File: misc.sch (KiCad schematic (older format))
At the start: 5 parts, among them J13 MICROSD_SLOT_TFP09-2-12B

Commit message: more schematics
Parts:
- added C? (x5): 10uF, symbol C_Small
- added P?: CONN_02X05, symbol CONN_02X05
- added P?: CONN_01X05, symbol CONN_01X05
- added R? (x5): 4K7, symbol RESISTOR
- added U?: 24LC256, symbol 24C16
- J13: footprint (none) -> geda-footprints:MICROSD_SLOT_TFP09-2-12B
- R32, R33, R34: footprint (none) -> Resistors_SMD:R_0603
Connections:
- net +3V3: now also P?.1 (P1), P?.2 (P2), P?.3 (P3), P?.4 (P4), P?.5 (P5), R?.1, R?.1, R?.1, R?.1, R?.1, U?.8 (VCC)
- net GND: now also C?.2, C?.2, C?.2, C?.2, C?.2, P?.10 (P10), P?.2 (P2), P?.4 (P4), P?.6 (P6), P?.8 (P8), U?.1 (A0), U?.2 (A1), U?.3 (A2), U?.4 (GND), U?.7 (WP)
- new net: C?.1, P?.1 (P1), R?.2
- new net: C?.1, P?.3 (P3), R?.2
- new net: C?.1, P?.5 (P5), R?.2
- new net: C?.1, P?.7 (P7), R?.2
- new net: C?.1, P?.9 (P9), R?.2

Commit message: More schematics, some layout
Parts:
- added C19, C20, C21, C22, C23, C24, C25: 100nF, Capacitors_SMD:C_0603, symbol C_Small
- added P13: EXT_SD, geda-footprints:CON_HDR_2x5, symbol CONN_02X05
- added P14: LCD, geda-footprints:CON_HDR_2x5, symbol CONN_02X05
- added P15: LIMIT_SWITCHES, geda-footprints:CON_HDR_2x7, symbol CONN_02X07
- added P16: LIMIT_SWITCHES_V, geda-footprints:CON_HDR_1x7, symbol CONN_01X07
- added P17, P18, P19, P20: CONN_01X03, geda-footprints:CON_HDR_1x3, symbol CONN_01X03
- added R35, R36: 4K7, Resistors_SMD:R_0603, symbol RESISTOR
- C26, C27, C28, C29, C30: renamed from C?; footprint (none) -> Capacitors_SMD:C_0805
- P21: renamed from P?; value CONN_02X05 -> THERMISTORS; footprint (none) -> geda-footprints:CON_HDR_2x5
- P22: renamed from P?; footprint (none) -> geda-footprints:CON_HDR_1x5
- R37, R38, R39, R40, R41: renamed from R?; footprint (none) -> Resistors_SMD:R_0603
- U2: renamed from U?; footprint (none) -> geda-footprints:SOIC8
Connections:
- net +3V3: now also P13.8 (P8), P16.1 (P1), P16.2 (P2), P16.3 (P3), P16.4 (P4), P16.5 (P5), P16.6 (P6), P16.7 (P7), P17.2 (P2), P18.2 (P2), P19.2 (P2), P20.2 (P2)
- net GND: now also C19.2, C20.2, C21.2, C22.2, C23.2, C24.2, C25.2, P13.2 (P2), P14.2 (P2), P15.10 (P10), P15.12 (P12), P15.14 (P14), P15.2 (P2), P15.4 (P4), P15.6 (P6), P15.8 (P8), P17.1 (P1), P18.1 (P1), P19.1 (P1), P20.1 (P1)
- net SD_CS: no longer J13.9 (CD0)
- net SD_MISO: now also P13.5 (P5)
- net SD_MOSI: now also P13.6 (P6)
- net SD_SCK: now also P13.4 (P4)
- net T0: now reaches C26.1, P21.1 (P1), R37.2
- net T1: now reaches C27.1, P21.3 (P3), R38.2
- net T2: now reaches C28.1, P21.5 (P5), R39.2
- net T3: now reaches C29.1, P21.7 (P7), R40.2
- net T4: now reaches C30.1, P21.9 (P9), R41.2
- net SDA1: now reaches U2.5 (SDA)
- net SDA1: now also R36.2
- net SCL1: now reaches U2.6 (SCL)
- net SCL1: now also R35.2
- new net: R35.1, R36.1
- new net +5V: P14.1 (P1)
- new net AUX-1: P17.3 (P3)
- new net AUX-2: P18.3 (P3)
- new net AUX-3: P19.3 (P3)
- new net AUX-4: P20.3 (P3)
- new net ENC-A: P14.3 (P3)
- new net ENC-B: P14.4 (P4)
- new net ENC-SW: P13.7 (P7)
- new net LCD_D4: P14.10 (P10)
- new net LCD_D5: P14.5 (P5)
- new net LCD_D6: P14.7 (P7)
- new net LCD_D7: P14.9 (P9)
- new net LCD_E: P14.8 (P8)
- new net LCD_RS: P14.6 (P6)
- new net PROBE: C19.1, P15.13 (P13)
- new net SD2_CS: P13.3 (P3)
- new net SD_CD: J13.9 (CD0)
- new net X+: C24.1, P15.3 (P3)
- new net X-: C25.1, P15.1 (P1)
- new net Y+: C22.1, P15.7 (P7)
- new net Y-: C23.1, P15.5 (P5)
- new net Z+: C20.1, P15.11 (P11)
- new net Z-: C21.1, P15.9 (P9)
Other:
- moved on the sheet: C26, C27, C28, C29, C30, P21, P22, R37, R38, R39, R40, R41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

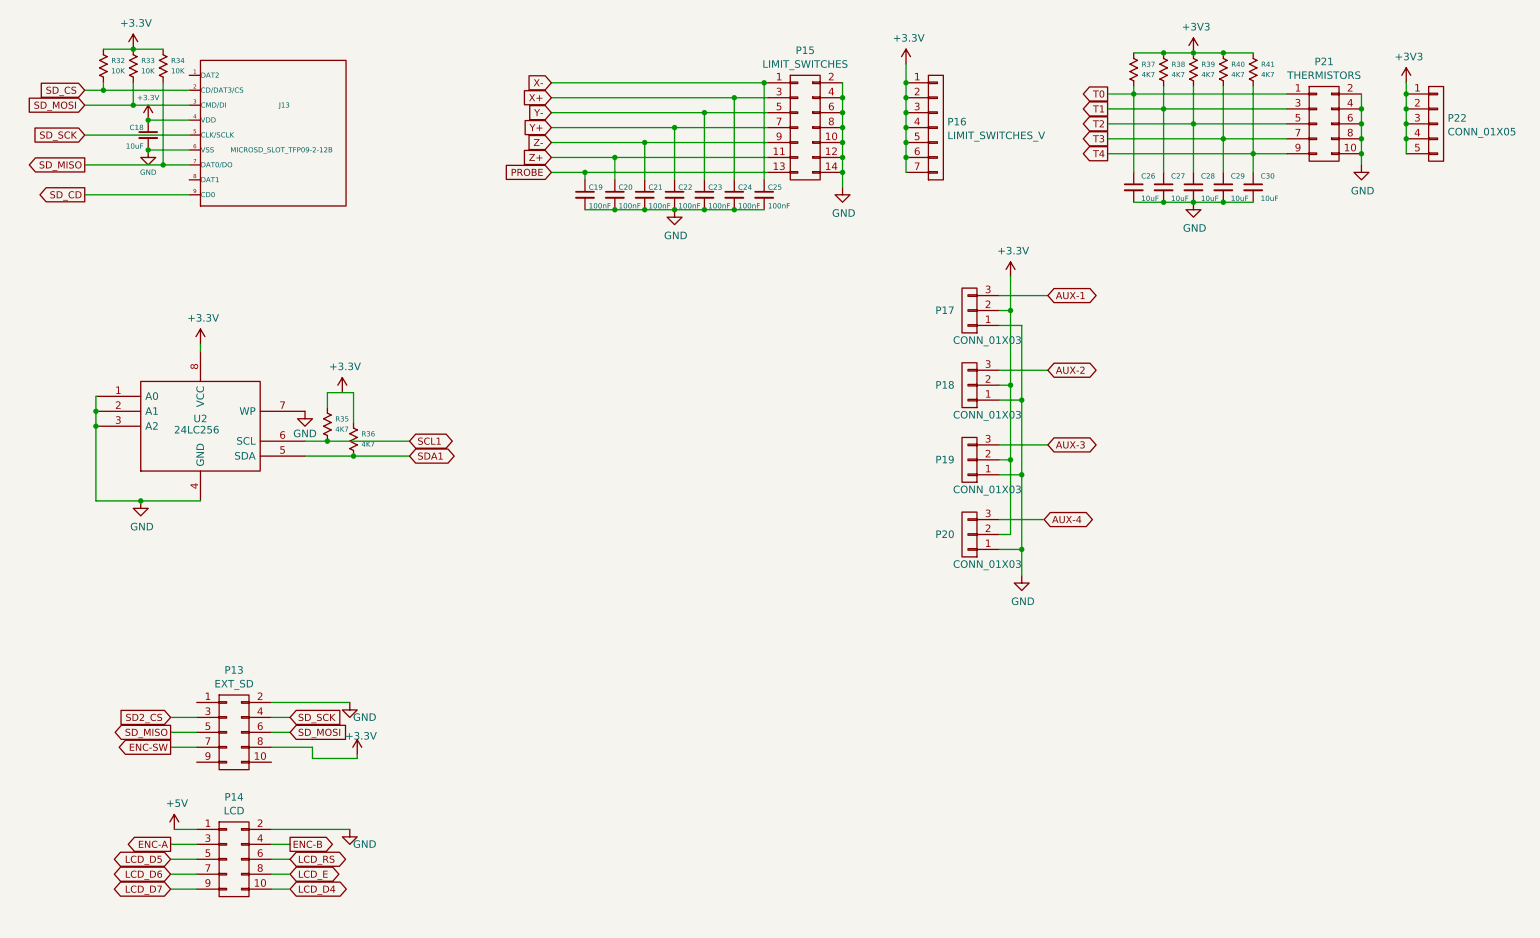
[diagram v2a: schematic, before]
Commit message: more placement and routing
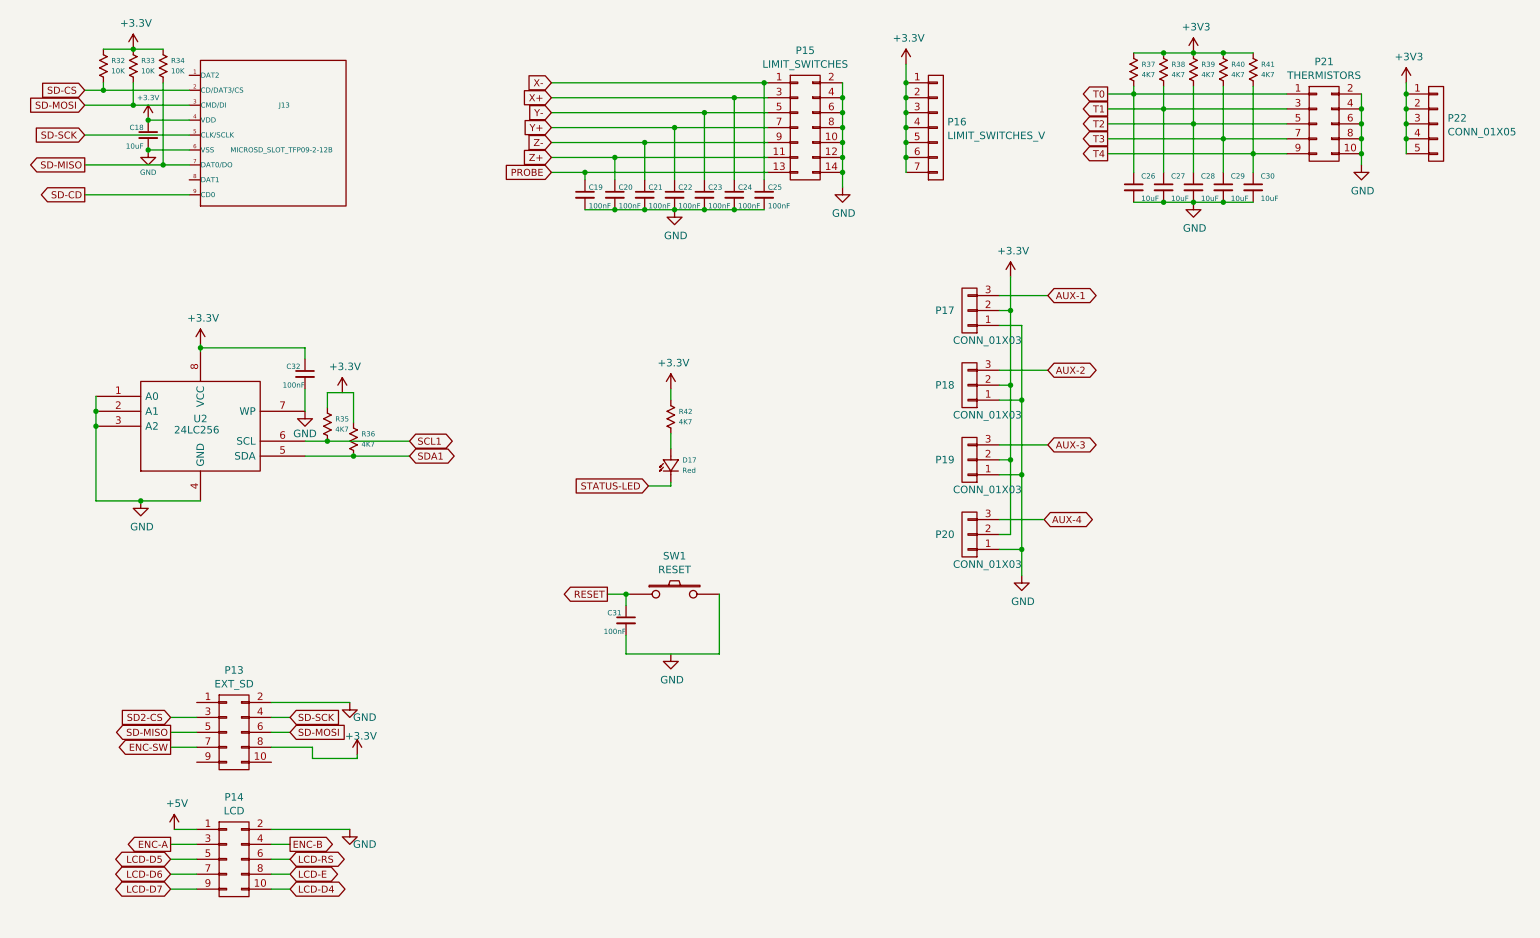
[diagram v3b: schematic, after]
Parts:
- added C31, C32: 100nF, Capacitors_SMD:C_0603, symbol C_Small
- added D17: Red, geda-footprints:0603diode, symbol Red
- added R42: 4K7, Resistors_SMD:R_0603, symbol RESISTOR
- added SW1: RESET, geda-footprints:BUTTON_PUSH_SMD_6x6mm, symbol SW_PUSH
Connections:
- net +3V3: now also C32.1, R42.1
- net GND: now also C32.2
- net LCD_D4 renamed LCD-D4
- net LCD_D5 renamed LCD-D5
- net LCD_D6 renamed LCD-D6
- net LCD_D7 renamed LCD-D7
- net LCD_E renamed LCD-E
- net LCD_RS renamed LCD-RS
- net SD2_CS renamed SD2-CS
- net SD_CD renamed SD-CD
- net SD_CS renamed SD-CS
- net SD_MISO renamed SD-MISO
- net SD_MOSI renamed SD-MOSI
- net SD_SCK renamed SD-SCK
- new net: D17.1 (null), R42.2
- new net: C31.2, SW1.2
- new net RESET: C31.1, SW1.1
- new net STATUS-LED: D17.2 (null)
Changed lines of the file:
@@
 EESchema Schematic File Version 2
+LIBS:led_reverse
 LIBS:arduino_shieldsNCL
 LIBS:otheruse_transistors
@@
 $EndDescr
 Text GLabel 1400 1575 0    47   Input ~ 0
-SD_CS
+SD-CS
 Text GLabel 1400 1675 0    47   Input ~ 0
-SD_MOSI
+SD-MOSI
 Text GLabel 1400 2075 0    47   Output ~ 0
-SD_MISO
+SD-MISO
 Text GLabel 1400 1875 0    47   Input ~ 0
-SD_SCK
+SD-SCK
 $Comp
 L RESISTOR R32
@@
 $EndComp
 $Comp
-L +3.3V #PWR074
+L +3.3V #PWR083
 U 1 1 568CFCD8
 P 1725 1300
-F 0 "#PWR074" H 1725 1150 50  0001 C CNN
+F 0 "#PWR083" H 1725 1150 50  0001 C CNN
 F 1 "+3.3V" H 1743 1474 50  0000 C CNN
 F 2 "" H 1725 1300 50  0000 C CNN
@@
 $EndComp
 $Comp
-L +3.3V #PWR075
+L +3.3V #PWR084
 U 1 1 568CFFAF
 P 1825 1775
-F 0 "#PWR075" H 1825 1625 50  0001 C CNN
+F 0 "#PWR084" H 1825 1625 50  0001 C CNN
 F 1 "+3.3V" H 1825 1925 35  0000 C CNN
 F 2 "" H 1825 1775 50  0000 C CNN
@@
 $EndComp
 Text GLabel 1400 2275 0    47   Output ~ 0
-SD_CD
+SD-CD
 $Comp
 L MICROSD_SLOT_TFP09-2-12B J13
@@
 $EndComp
 $Comp
-L GND #PWR076
+L GND #PWR085
 U 1 1 568C59D5
 P 1825 1975
-F 0 "#PWR076" H 1825 1725 50  0001 C CNN
+F 0 "#PWR085" H 1825 1725 50  0001 C CNN
 F 1 "GND" H 1825 1825 35  0000 C CNN
 F 2 "" H 1825 1975 50  0000 C CNN
@@
 $EndComp
 $Comp
-L GND #PWR077
+L GND #PWR086
 U 1 1 568D834C
 P 9950 2075
-F 0 "#PWR077" H 9950 1825 50  0001 C CNN
+F 0 "#PWR086" H 9950 1825 50  0001 C CNN
 F 1 "GND" H 9958 1901 50  0000 C CNN
 F 2 "" H 9950 2075 50  0000 C CNN
@@
 $EndComp
 $Comp
-L GND #PWR078
+L GND #PWR087
 U 1 1 568D94E5
 P 8825 2325
-F 0 "#PWR078" H 8825 2075 50  0001 C CNN
+F 0 "#PWR087" H 8825 2075 50  0001 C CNN
 F 1 "GND" H 8833 2151 50  0000 C CNN
 F 2 "" H 8825 2325 50  0000 C CNN
@@
 $EndComp
 $Comp
-L +3V3 #PWR079
+L +3V3 #PWR088
 U 1 1 568D9512
 P 8825 1325
-F 0 "#PWR079" H 8825 1175 50  0001 C CNN
+F 0 "#PWR088" H 8825 1175 50  0001 C CNN
 F 1 "+3V3" H 8843 1499 50  0000 C CNN
 F 2 "" H 8825 1325 50  0000 C CNN
@@
 $EndComp
 $Comp
-L +3V3 #PWR080
+L +3V3 #PWR089
 U 1 1 568D9A56
 P 10250 1525
-F 0 "#PWR080" H 10250 1375 50  0001 C CNN
+F 0 "#PWR089" H 10250 1375 50  0001 C CNN
 F 1 "+3V3" H 10268 1699 50  0000 C CNN
 F 2 "" H 10250 1525 50  0000 C CNN
@@
 $EndComp
 $Comp
-L GND #PWR081
+L GND #PWR090
 U 1 1 568DA443
 P 2875 3725
-F 0 "#PWR081" H 2875 3475 50  0001 C CNN
+F 0 "#PWR090" H 2875 3475 50  0001 C CNN
 F 1 "GND" H 2875 3575 50  0000 C CNN
 F 2 "" H 2875 3725 50  0000 C CNN
@@
 $EndComp
 $Comp
-L GND #PWR082
+L GND #PWR091
 U 1 1 568DA52A
 P 1775 4325
-F 0 "#PWR082" H 1775 4075 50  0001 C CNN
+F 0 "#PWR091" H 1775 4075 50  0001 C CNN
 F 1 "GND" H 1783 4151 50  0000 C CNN
 F 2 "" H 1775 4325 50  0000 C CNN
@@
 $EndComp
 $Comp
-L +3.3V #PWR083
+L +3.3V #PWR092
 U 1 1 568DA65A
 P 2175 3275
-F 0 "#PWR083" H 2175 3125 50  0001 C CNN
+F 0 "#PWR092" H 2175 3125 50  0001 C CNN
 F 1 "+3.3V" H 2193 3449 50  0000 C CNN
 F 2 "" H 2175 3275 50  0000 C CNN
@@
 $EndComp
 $Comp
-L GND #PWR084
+L GND #PWR093
 U 1 1 568D90A7
 P 6475 2225
-F 0 "#PWR084" H 6475 1975 50  0001 C CNN
+F 0 "#PWR093" H 6475 1975 50  0001 C CNN
 F 1 "GND" H 6483 2051 50  0000 C CNN
 F 2 "" H 6475 2225 50  0000 C CNN
@@
 $EndComp
 $Comp
-L +3.3V #PWR085
+L +3.3V #PWR094
 U 1 1 568D9133
 P 6900 1400
-F 0 "#PWR085" H 6900 1250 50  0001 C CNN
+F 0 "#PWR094" H 6900 1250 50  0001 C CNN
 F 1 "+3.3V" H 6918 1574 50  0000 C CNN
 F 2 "" H 6900 1400 50  0000 C CNN
@@
 $EndComp
 $Comp
-L GND #PWR086
+L GND #PWR095
 U 1 1 568DAACD
 P 5350 2375
-F 0 "#PWR086" H 5350 2125 50  0001 C CNN
+F 0 "#PWR095" H 5350 2125 50  0001 C CNN
 F 1 "GND" H 5358 2201 50  0000 C CNN
 F 2 "" H 5350 2375 50  0000 C CNN
@@
 $EndComp
 $Comp
-L +3.3V #PWR087
+L +3.3V #PWR096
 U 1 1 568E82EF
 P 3125 3600
-F 0 "#PWR087" H 3125 3450 50  0001 C CNN
+F 0 "#PWR096" H 3125 3450 50  0001 C CNN
 F 1 "+3.3V" H 3143 3774 50  0000 C CNN
 F 2 "" H 3125 3600 50  0000 C CNN
@@
 	7600 4550 7525 4550
 $Comp
-L GND #PWR088
+L GND #PWR097
 U 1 1 568EABC9
 P 7675 4825
-F 0 "#PWR088" H 7675 4575 50  0001 C CNN
+F 0 "#PWR097" H 7675 4575 50  0001 C CNN
 F 1 "GND" H 7683 4651 50  0000 C CNN
 F 2 "" H 7675 4825 50  0000 C CNN
@@
 $EndComp
 $Comp
-L +3.3V #PWR089
+L +3.3V #PWR098
 U 1 1 568EAEBC
 P 7600 2825
-F 0 "#PWR089" H 7600 2675 50  0001 C CNN
+F 0 "#PWR098" H 7600 2675 50  0001 C CNN
 F 1 "+3.3V" H 7618 2999 50  0000 C CNN
 F 2 "" H 7600 2825 50  0000 C CNN
@@
 $EndComp
 Text GLabel 1975 5775 0    47   Input ~ 0
-SD2_CS
+SD2-CS
 Text GLabel 2775 5875 2    47   Input ~ 0
-SD_MOSI
+SD-MOSI
 Text GLabel 1975 5875 0    47   Output ~ 0
-SD_MISO
+SD-MISO
 Text GLabel 2775 5775 2    47   Input ~ 0
-SD_SCK
-$Comp
-L GND #PWR090
+SD-SCK
+$Comp
+L GND #PWR099
 U 1 1 568F027E
 P 3175 5675
-F 0 "#PWR090" H 3175 5425 50  0001 C CNN
+F 0 "#PWR099" H 3175 5425 50  0001 C CNN
 F 1 "GND" H 3275 5575 50  0000 C CNN
 F 2 "" H 3175 5675 50  0000 C CNN
@@
 	2650 5675 3175 5675
 $Comp
-L +3.3V #PWR091
+L +3.3V #PWR0100
 U 1 1 568F1103
 P 3225 6025
-F 0 "#PWR091" H 3225 5875 50  0001 C CNN
+F 0 "#PWR0100" H 3225 5875 50  0001 C CNN
 F 1 "+3.3V" H 3250 6150 50  0000 C CNN
 F 2 "" H 3225 6025 50  0000 C CNN
@@
 	3225 6050 3225 6025
 $Comp
-L +5V #PWR092
+L +5V #PWR0101
 U 1 1 568F17B3
 P 2000 6525
-F 0 "#PWR092" H 2000 6375 50  0001 C CNN
+F 0 "#PWR0101" H 2000 6375 50  0001 C CNN
 F 1 "+5V" H 2018 6699 50  0000 C CNN
 F 2 "" H 2000 6525 50  0000 C CNN
@@
 $EndComp
 $Comp
-L GND #PWR093
+L GND #PWR0102
 U 1 1 568F18BA
 P 3175 6525
-F 0 "#PWR093" H 3175 6275 50  0001 C CNN
+F 0 "#PWR0102" H 3175 6275 50  0001 C CNN
 F 1 "GND" H 3275 6425 50  0000 C CNN
 F 2 "" H 3175 6525 50  0000 C CNN
@@
 	2150 6625 1975 6625
 Text GLabel 1975 6725 0    47   BiDi ~ 0
-LCD_D5
+LCD-D5
 Text GLabel 1975 6825 0    47   BiDi ~ 0
-LCD_D6
+LCD-D6
 Text GLabel 1975 6925 0    47   BiDi ~ 0
-LCD_D7
+LCD-D7
 Text GLabel 2775 6925 2    47   BiDi ~ 0
-LCD_D4
+LCD-D4
 Text GLabel 2775 6825 2    47   BiDi ~ 0
-LCD_E
+LCD-E
 Text GLabel 2775 6725 2    47   BiDi ~ 0
-LCD_RS
+LCD-RS
 Wire Wire Line
 	1975 6725 2150 6725
@@
 Text GLabel 8250 2000 0    47   Output ~ 0
 T4
+$Comp
+L Red D17
+U 1 1 568F7EEA
+P 5375 4200
+F 0 "D17" V 5523 4173 34  0000 R CNN
+F 1 "Red" V 5454 4173 34  0000 R CNN
+F 2 "geda-footprints:0603diode" H 5375 4200 60  0001 C CNN
+F 3 "" H 5375 4200 60  0000 C CNN
+	1    5375 4200
+	0    -1   -1   0
+$EndComp
+$Comp
+L SW_PUSH SW1
+U 1 1 568F83A9
+P 5350 4950
+F 0 "SW1" H 5350 5206 50  0000 C CNN
+F 1 "RESET" H 5350 5114 50  0000 C CNN
+F 2 "geda-footprints:BUTTON_PUSH_SMD_6x6mm" H 5350 4950 50  0001 C CNN
+F 3 "" H 5350 4950 50  0000 C CNN
+	1    5350 4950
+	1    0    0    -1
+$EndComp
+Text GLabel 5175 4225 0    47   Input ~ 0
+STATUS-LED
+$Comp
+L RESISTOR R42
+U 1 1 568F903C
+P 5300 3650
+F 0 "R42" V 5377 3728 34  0000 L CNN
+F 1 "4K7" V 5446 3728 34  0000 L CNN
+F 2 "Resistors_SMD:R_0603" H 5300 3650 60  0001 C CNN
+F 3 "" H 5300 3650 60  0000 C CNN
+	1    5300 3650
+	0    1    1    0
+$EndComp
+Wire Wire Line
+	5325 3875 5325 3975
+Wire Wire Line
+	5175 4225 5325 4225
+Wire Wire Line
+	5325 4225 5325 4200
+$Comp
+L +3.3V #PWR0103
+U 1 1 568F9643
+P 5325 3575
+F 0 "#PWR0103" H 5325 3425 50  0001 C CNN
+F 1 "+3.3V" H 5343 3749 50  0000 C CNN
+F 2 "" H 5325 3575 50  0000 C CNN
+F 3 "" H 5325 3575 50  0000 C CNN
+	1    5325 3575
+	1    0    0    -1
+$EndComp
+Wire Wire Line
+	5325 3575 5325 3650
+Text GLabel 4900 4950 0    47   Output ~ 0
+RESET
+Wire Wire Line
+	4900 4950 5050 4950
+$Comp
+L GND #PWR0104
+U 1 1 568F9E88
+P 5325 5350
+F 0 "#PWR0104" H 5325 5100 50  0001 C CNN
+F 1 "GND" H 5333 5176 50  0000 C CNN
+F 2 "" H 5325 5350 50  0000 C CNN
+F 3 "" H 5325 5350 50  0000 C CNN
+	1    5325 5350
+	1    0    0    -1
+$EndComp
+$Comp
+L C_Small C31
+U 1 1 568FA294
+P 5025 5125
+F 0 "C31" H 4900 5175 35  0000 L CNN
+F 1 "100nF" H 4875 5050 35  0000 L CNN
+F 2 "Capacitors_SMD:C_0603" H 5025 5125 50  0001 C CNN
+F 3 "" H 5025 5125 50  0000 C CNN
+	1    5025 5125
+	1    0    0    -1
+$EndComp
+Wire Wire Line
+	5025 5025 5025 4950
+Connection ~ 5025 4950
+Wire Wire Line
+	5025 5225 5025 5350
+Wire Wire Line
+	5025 5350 5650 5350
+Wire Wire Line
+	5650 5350 5650 4950
+$Comp
+L C_Small C32
+U 1 1 568FAA2A
+P 2875 3475
+F 0 "C32" H 2750 3525 35  0000 L CNN
+F 1 "100nF" H 2725 3400 35  0000 L CNN
+F 2 "Capacitors_SMD:C_0603" H 2875 3475 50  0001 C CNN
+F 3 "" H 2875 3475 50  0000 C CNN
+	1    2875 3475
+	1    0    0    -1
+$EndComp
+Wire Wire Line
+	2875 3575 2875 3725
+Wire Wire Line
+	2875 3300 2875 3375
+Wire Wire Line
+	2875 3300 2175 3300
+Connection ~ 2175 3300
 $EndSCHEMATC

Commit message: More routing
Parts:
- added C33: 10uF, Capacitors_SMD:C_0805, symbol C_Small
- D17: footprint geda-footprints:0603diode -> armin-footprints:0603diode
- U2: footprint geda-footprints:SOIC8 -> armin-footprints:SOIC8
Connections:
- net +3V3: now also P17.1 (P1), P18.1 (P1), P19.1 (P1), P20.1 (P1), R35.1, R36.1, C33.1; no longer P17.2 (P2), P18.2 (P2), P19.2 (P2), P20.2 (P2)
- net GND: now also P17.2 (P2), P18.2 (P2), P19.2 (P2), P20.2 (P2), C33.2; no longer P17.1 (P1), P18.1 (P1), P19.1 (P1), P20.1 (P1)
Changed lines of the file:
@@
 F 0 "U2" H 2175 3875 50  0000 C CNN
 F 1 "24LC256" H 2150 3800 50  0000 C CNN
-F 2 "geda-footprints:SOIC8" H 2175 3825 50  0001 C CNN
+F 2 "armin-footprints:SOIC8" H 2175 3825 50  0001 C CNN
 F 3 "" H 2175 3825 50  0000 C CNN
 	1    2175 3825
@@
 U 1 1 568D8D39
 P 6225 1825
-F 0 "P15" H 6225 2341 50  0000 C CNN
-F 1 "LIMIT_SWITCHES" H 6225 2249 50  0000 C CNN
+F 0 "P15" H 6225 2300 50  0000 C CNN
+F 1 "LIMIT_SWITCHES" H 6100 2225 50  0000 C CNN
 F 2 "geda-footprints:CON_HDR_2x7" H 6225 625 50  0001 C CNN
 F 3 "" H 6225 625 50  0000 C CNN
@@
 $EndComp
 Wire Wire Line
-	7600 2825 7600 4550
+	7600 3050 7600 4800
 Wire Wire Line
 	7525 3150 7675 3150
 Wire Wire Line
-	7675 3150 7675 4825
+	7675 2825 7675 4650
 Wire Wire Line
 	7525 3650 7675 3650
@@
 Connection ~ 7675 4150
 Wire Wire Line
-	7525 4650 7675 4650
-Connection ~ 7675 4650
+	7675 4650 7525 4650
 Wire Wire Line
 	7600 3050 7525 3050
@@
 L GND #PWR097
 U 1 1 568EABC9
-P 7675 4825
-F 0 "#PWR097" H 7675 4575 50  0001 C CNN
-F 1 "GND" H 7683 4651 50  0000 C CNN
-F 2 "" H 7675 4825 50  0000 C CNN
-F 3 "" H 7675 4825 50  0000 C CNN
-	1    7675 4825
+P 7600 4800
+F 0 "#PWR097" H 7600 4550 50  0001 C CNN
+F 1 "GND" H 7608 4626 50  0000 C CNN
+F 2 "" H 7600 4800 50  0000 C CNN
+F 3 "" H 7600 4800 50  0000 C CNN
+	1    7600 4800
 	1    0    0    -1
 $EndComp
@@
 L +3.3V #PWR098
 U 1 1 568EAEBC
-P 7600 2825
-F 0 "#PWR098" H 7600 2675 50  0001 C CNN
-F 1 "+3.3V" H 7618 2999 50  0000 C CNN
-F 2 "" H 7600 2825 50  0000 C CNN
-F 3 "" H 7600 2825 50  0000 C CNN
-	1    7600 2825
+P 7675 2825
+F 0 "#PWR098" H 7675 2675 50  0001 C CNN
+F 1 "+3.3V" H 7693 2999 50  0000 C CNN
+F 2 "" H 7675 2825 50  0000 C CNN
+F 3 "" H 7675 2825 50  0000 C CNN
+	1    7675 2825
 	1    0    0    -1
 $EndComp
@@
 Wire Wire Line
 	7525 4450 7825 4450
-Connection ~ 7600 3050
 $Comp
 L CONN_02X05 P13
@@
 F 0 "D17" V 5523 4173 34  0000 R CNN
 F 1 "Red" V 5454 4173 34  0000 R CNN
-F 2 "geda-footprints:0603diode" H 5375 4200 60  0001 C CNN
+F 2 "armin-footprints:0603diode" H 5375 4200 60  0001 C CNN
 F 3 "" H 5375 4200 60  0000 C CNN
 	1    5375 4200
@@
 	2875 3300 2175 3300
 Connection ~ 2175 3300
+Connection ~ 7675 3150
+Connection ~ 7600 4550
+Connection ~ 3125 3600
+$Comp
+L C_Small C33
+U 1 1 56943D4C
+P 6475 1425
+F 0 "C33" H 6500 1475 35  0000 L CNN
+F 1 "10uF" H 6500 1350 35  0000 L CNN
+F 2 "Capacitors_SMD:C_0805" H 6475 1425 50  0001 C CNN
+F 3 "" H 6475 1425 50  0000 C CNN
+	1    6475 1425
+	1    0    0    -1
+$EndComp
+$Comp
+L +3.3V #PWR0105
+U 1 1 56944144
+P 6475 1275
+F 0 "#PWR0105" H 6475 1125 50  0001 C CNN
+F 1 "+3.3V" H 6493 1449 50  0000 C CNN
+F 2 "" H 6475 1275 50  0000 C CNN
+F 3 "" H 6475 1275 50  0000 C CNN
+	1    6475 1275
+	1    0    0    -1
+$EndComp
+Wire Wire Line
+	6475 1275 6475 1325
 $EndSCHEMATC
